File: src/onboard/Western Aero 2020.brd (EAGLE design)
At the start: 112.2 x 92.9 mm, 84 parts, among them J1 PITOT, J10 ANA_IO, J11 PWR, J2 BUZZER, J3 RX2/TX2, J4 RX3/TX3, J5 SPI, J6 DIG_IO, J7 RX1/TX1, J8 DIG_IO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

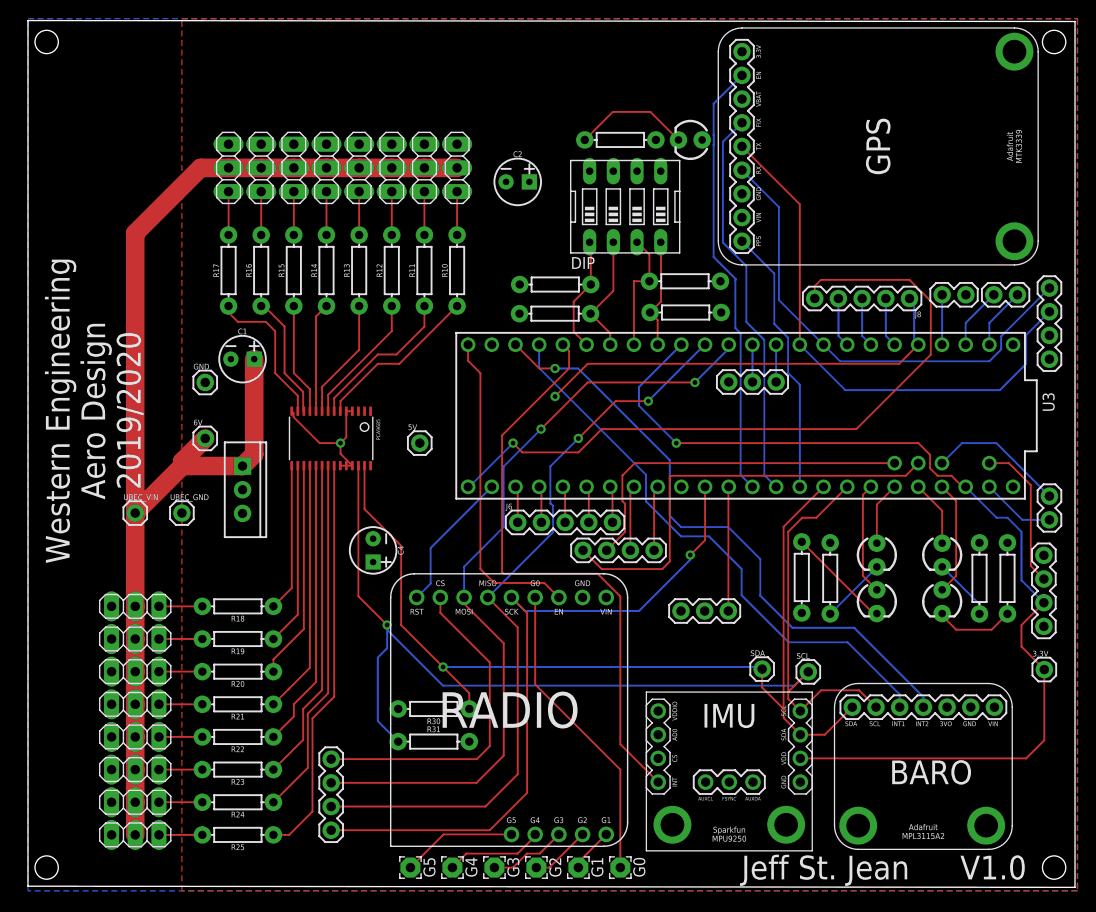
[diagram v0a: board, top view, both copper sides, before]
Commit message: Fixed some connections and upgraded to ver 2.0
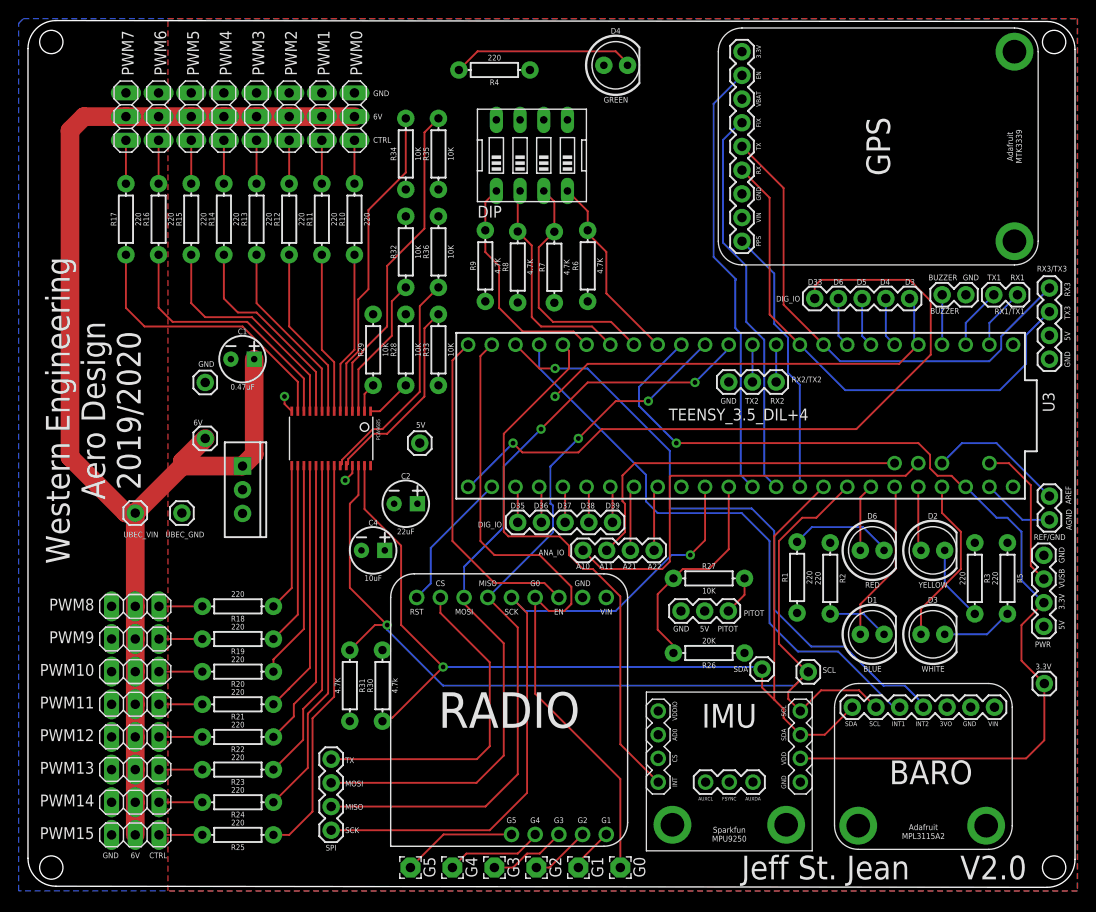
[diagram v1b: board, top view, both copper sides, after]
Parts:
- removed D5: Green, SparkFun-LED:LED_3MM
- added D6: RED, SparkFun-LED:LED_5MM
- added R26: 20K, SparkFun-Resistors:AXIAL-0.3
- added R27, R28, R29, R32, R33, R34, R35, R36: 10K, SparkFun-Resistors:AXIAL-0.3
- D1: value Red -> BLUE; device SparkFun-LED:LED_3MM -> SparkFun-LED:LED_5MM
- D2: value Blue -> YELLOW; device SparkFun-LED:LED_3MM -> SparkFun-LED:LED_5MM
- D3: value Yellow -> WHITE; device SparkFun-LED:LED_3MM -> SparkFun-LED:LED_5MM
- D4: value White -> GREEN; device SparkFun-LED:LED_3MM -> SparkFun-LED:LED_5MM
- R6, R7, R8, R9: value 10K -> 4.7K
- moved D4 67.3 mm to (65.0, 88.5), turned to 0 degrees
- moved C2 36.5 mm to (42.5, 41.5)
- moved R4 15.4 mm to (52.0, 88.0)
- moved R7 14.1 mm to (58.4, 66.8), turned to 90 degrees
- moved JP1 12.3 mm to (37.0, 83.0)
- moved JP2 12.3 mm to (33.5, 83.0)
- moved JP3 12.3 mm to (30.0, 83.0)
- moved JP4 12.3 mm to (26.5, 83.0)
- moved JP5 12.3 mm to (23.0, 83.0)
- moved JP6 12.3 mm to (19.5, 83.0)
- moved JP7 12.3 mm to (16.0, 83.0)
- moved JP8 12.3 mm to (12.5, 83.0)
- moved R10 12.3 mm to (37.0, 72.0)
- moved R11 12.3 mm to (33.5, 72.0)
- moved R12 12.3 mm to (30.0, 72.0)
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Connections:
- new net N$28: J1.3, R27.P$2
- new net N$29: PCA9685.24, R33.P$2
- new net N$30: PCA9685.23, R36.P$1
- new net N$31: PCA9685.5, R34.P$2
- new net N$32: PCA9685.4, R35.P$2
- new net N$33: PCA9685.3, R32.P$1
- new net N$34: PCA9685.2, R29.P$1
- net 5V: now also D4.A, DIP.5, DIP.6, DIP.7, DIP.8, R28.P$2, R29.P$2, R32.P$2; no longer D5.A, PCA9685.1, PCA9685.2, PCA9685.3
- net BLUE_LED: now also D1.A; no longer D2.A
- net GND: now also R26.P$1, R33.P$1, R34.P$1, R35.P$1, R36.P$2, U1.GND; no longer DIP.5, DIP.6, DIP.7, DIP.8, PCA9685.23, PCA9685.24, PCA9685.4, PCA9685.5
- net LORA_INT: now also G0.1, U8.4
- net N$2: now also D6.K; no longer D1.K
- net N$27: now also PCA9685.1, R28.P$1; no longer G0.1, U8.4
- net N$3: now also D1.K; no longer D2.K
- net N$4: now also D2.K; no longer D3.K
- net N$5: now also D3.K; no longer D4.K
- net N$6: now also D4.K; no longer D5.K
- net PITOT: now also R26.P$2, R27.P$1; no longer J1.3
- net RED_LED: now also D6.A; no longer D1.A
- net RX3: now also U9.TX; no longer U9.RX
- net TX3: now also U9.RX; no longer U9.TX
- net WHITE_LED: now also D3.A; no longer D4.A
- net YELLOW_LED: now also D2.A; no longer D3.A
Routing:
- net LORA_INT: track 0.00 -> 72.7 mm
- net N$32: track 0.00 -> 35.2 mm
- net N$31: track 0.00 -> 34.0 mm
- net N$27: track 32.7 -> 4.92 mm
- net N$30: track 0.00 -> 24.1 mm
- net N$29: track 0.00 -> 21.2 mm
- net N$33: track 0.00 -> 15.4 mm
- net PWM6: track 13.3 -> 27.9 mm
- net PWM7: track 16.1 -> 30.6 mm
- net PWM5: track 12.0 -> 25.0 mm
- net DIP2: track 13.2 -> 25.5 mm
- net DIP4: track 12.4 -> 24.6 mm
- net GND: track 15.5 -> 3.81 mm, vias 1 -> 2
- net DIP3: track 12.9 -> 23.9 mm
- net BLUE_LED: track 6.83 -> 17.4 mm
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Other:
- outline, holes or cut-outs redrawn
- board text added: "3.3V"
- board text added: "5V"
- board text added: "6V"
- board text added: "A10"
- board text added: "A11"
- board text added: "A21"
- board text added: "A22"
- board text added: "AGND"
- board text added: "AREF"
- board text added: "BUZZER"
- board text added: "CTRL"
- board text added: "D3"
- board text added: "D33"
- board text added: "D35"
- board text added: "D36"
- board text added: "D37"
- board text added: "D38"
- board text added: "D39"
- board text added: "D4"
- board text added: "D5"
- board text added: "D6"
- board text added: "GND"
- board text added: "I feel the need... The need for speed"
- board text added: "It's Time To Buzz The Tower"
- board text added: "MISO"
- board text added: "MOSI"
- board text added: "PITOT"
- board text added: "RX1"
- board text added: "RX2"
- board text added: "RX3"
- board text added: "SCK"
- board text added: "TX"
- board text added: "TX1"
- board text added: "TX2"
- board text added: "TX3"
- board text added: "V2.0"
- board text added: "VUSB"
- board text removed: "V1.0"

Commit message: Added larger mounting holes and cleaned up silk screen
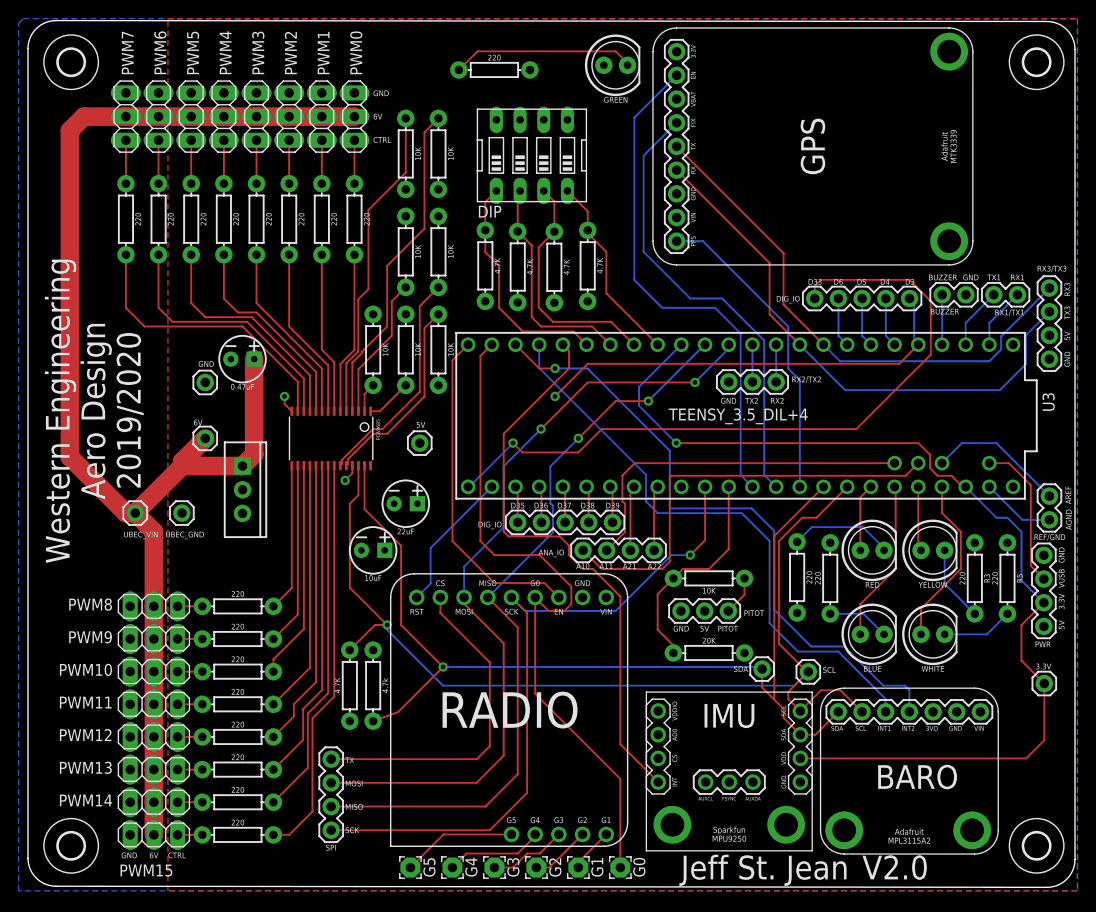
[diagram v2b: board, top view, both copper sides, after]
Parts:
- added H1, H2, H3, H4: MOUNT-HOLE2.8, holes:2,8
- moved U9 7.00 mm to (69.0, 92.5)
- moved JP10 2.00 mm to (15.5, 27.0)
- moved JP11 2.00 mm to (15.5, 23.5)
- moved JP12 2.00 mm to (15.5, 20.0)
- moved JP13 2.00 mm to (15.5, 16.5)
- moved JP14 2.00 mm to (15.5, 13.0)
- moved JP15 2.00 mm to (15.5, 9.50)
- moved JP16 2.00 mm to (15.5, 6.00)
- moved JP9 2.00 mm to (15.5, 30.5)
- moved U6 1.58 mm to (106.0, 21.7)
- moved R30 1.00 mm to (39.0, 22.0)
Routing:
- net GPS_EN: track 47.2 -> 54.5 mm
- net GPS_FIX: track 42.4 -> 48.4 mm
- net GPS_PPS: track 28.9 -> 33.4 mm
- net TX3: track 55.3 -> 58.2 mm
- net RX3: track 53.9 -> 56.8 mm
- net N$24: track 4.65 -> 2.65 mm
- net N$23: track 4.65 -> 2.65 mm
- net N$22: track 4.65 -> 2.65 mm
- net N$21: track 4.65 -> 2.65 mm
- net N$20: track 4.65 -> 2.65 mm
- net N$19: track 4.65 -> 2.65 mm
- net N$18: track 4.65 -> 2.65 mm
- net N$17: track 4.65 -> 2.65 mm
- net SCL: track 113.5 -> 112.2 mm
- net SDA: track 108.7 -> 107.9 mm
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
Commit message: Release v2.0
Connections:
- removed net TX_2: J5.4, U8.8
- net TX2: now also J5.4, U8.8
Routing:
- net TX2: track 4.00 -> 91.5 mm, vias 0 -> 1
- net TX_2: track 35.7 -> 0.00 mm
- net MISO: track 80.8 -> 82.9 mm
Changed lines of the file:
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@@
 <drawing>
 <settings>
-<setting alwaysvectorfont="yes"/>
+<setting alwaysvectorfont="no"/>
 <setting verticaltext="up"/>
 </settings>
@@
 <wire x1="58.275" y1="41.3" x2="58.075" y2="41.5" width="0.2032" layer="16"/>
 <wire x1="58.075" y1="41.5" x2="58" y2="41.5" width="0.2032" layer="16"/>
-<wire x1="58" y1="41.5" x2="58" y2="45.5" width="0.2032" layer="16"/>
-<wire x1="58" y1="45.5" x2="61" y2="48.5" width="0.2032" layer="16"/>
-<via x="61" y="48.5" extent="1-16" drill="0.508"/>
-<wire x1="61" y1="48.5" x2="65" y2="52.5" width="0.2032" layer="1"/>
-<wire x1="65" y1="52.5" x2="68.5" y2="52.5" width="0.2032" layer="1"/>
+<wire x1="58" y1="41.5" x2="58" y2="46.5" width="0.2032" layer="16"/>
+<wire x1="59" y1="47.5" x2="58" y2="46.5" width="0.2032" layer="16"/>
+<wire x1="59" y1="47.5" x2="59" y2="50" width="0.2032" layer="16"/>
+<via x="59" y="50" extent="1-16" drill="0.508"/>
+<wire x1="59" y1="50" x2="60" y2="51" width="0.2032" layer="1"/>
+<wire x1="61.5" y1="51" x2="60" y2="51" width="0.2032" layer="1"/>
+<wire x1="63" y1="52.5" x2="61.5" y2="51" width="0.2032" layer="1"/>
+<wire x1="63" y1="52.5" x2="68.5" y2="52.5" width="0.2032" layer="1"/>
 <via x="68.5" y="52.5" extent="1-16" drill="0.508"/>
 <wire x1="68.5" y1="52.5" x2="74.55" y2="58.55" width="0.2032" layer="16"/>
@@
 <wire x1="79.665" y1="54.55" x2="79.66" y2="54.555" width="0.2032" layer="16"/>
 <wire x1="79.66" y1="54.555" x2="79.66" y2="58.55" width="0.2032" layer="16"/>
+<contactref element="U8" pad="8"/>
+<wire x1="79.665" y1="54.55" x2="75.44" y2="50.325" width="0.2032" layer="1"/>
+<wire x1="61.825" y1="50.325" x2="60.5" y2="49" width="0.2032" layer="1"/>
+<via x="60.5" y="49" extent="1-16" drill="0.508"/>
+<wire x1="60.5" y1="40.34013125" x2="60.8246" y2="40.01553125" width="0.2032" layer="16"/>
+<wire x1="60.8246" y1="40.01553125" x2="60.8246" y2="38.98446875" width="0.2032" layer="16"/>
+<wire x1="60.8246" y1="38.98446875" x2="60.775" y2="38.93486875" width="0.2032" layer="16"/>
+<wire x1="60.775" y1="38.93486875" x2="60.775" y2="38.4" width="0.2032" layer="16"/>
+<wire x1="53.35655" y1="32.593" x2="52.687" y2="31.92345" width="0.2032" layer="16"/>
+<wire x1="60.775" y1="38.4" x2="54.968" y2="32.593" width="0.2032" layer="16"/>
+<wire x1="52.687" y1="30.312" x2="52.375" y2="30" width="0.2032" layer="16"/>
+<wire x1="54.968" y1="32.593" x2="53.35655" y2="32.593" width="0.2032" layer="16"/>
+<wire x1="52.687" y1="31.92345" x2="52.687" y2="30.312" width="0.2032" layer="16"/>
+<wire x1="47.66" y1="30" x2="46.21" y2="31.45" width="0.2032" layer="16"/>
+<wire x1="75.44" y1="50.325" x2="61.825" y2="50.325" width="0.2032" layer="1"/>
+<wire x1="60.5" y1="49" x2="60.5" y2="40.34013125" width="0.2032" layer="16"/>
+<wire x1="52.375" y1="30" x2="47.66" y2="30" width="0.2032" layer="16"/>
+<contactref element="J5" pad="4"/>
+<wire x1="34.5" y1="14.12" x2="50.12" y2="14.12" width="0.2032" layer="1"/>
+<wire x1="50.12" y1="14.12" x2="51.5" y2="15.5" width="0.2032" layer="1"/>
+<wire x1="51.5" y1="15.5" x2="51.5" y2="24.5" width="0.2032" layer="1"/>
+<wire x1="51.5" y1="24.5" x2="46.21" y2="29.79" width="0.2032" layer="1"/>
+<wire x1="46.21" y1="29.79" x2="46.21" y2="31.45" width="0.2032" layer="1"/>
 </signal>
 <signal name="LORA_EN">
@@
 <wire x1="64.66" y1="43.07" x2="64.42" y2="43.31" width="0.2032" layer="1"/>
 </signal>
-<signal name="TX_2">
-<contactref element="U8" pad="8"/>
-<contactref element="J5" pad="4"/>
-<wire x1="34.5" y1="14.12" x2="50.12" y2="14.12" width="0.2032" layer="1"/>
-<wire x1="50.12" y1="14.12" x2="51.5" y2="15.5" width="0.2032" layer="1"/>
-<wire x1="51.5" y1="15.5" x2="51.5" y2="24.5" width="0.2032" layer="1"/>
-<wire x1="46.21" y1="29.79" x2="46.21" y2="31.45" width="0.2032" layer="1"/>
-<wire x1="51.5" y1="24.5" x2="46.21" y2="29.79" width="0.2032" layer="1"/>
-</signal>
 <signal name="D33">
